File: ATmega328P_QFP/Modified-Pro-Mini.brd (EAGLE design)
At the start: 18.3 x 33.5 mm, 17 parts, among them Q1 8/16/20MHz, U1 ATMEGA328

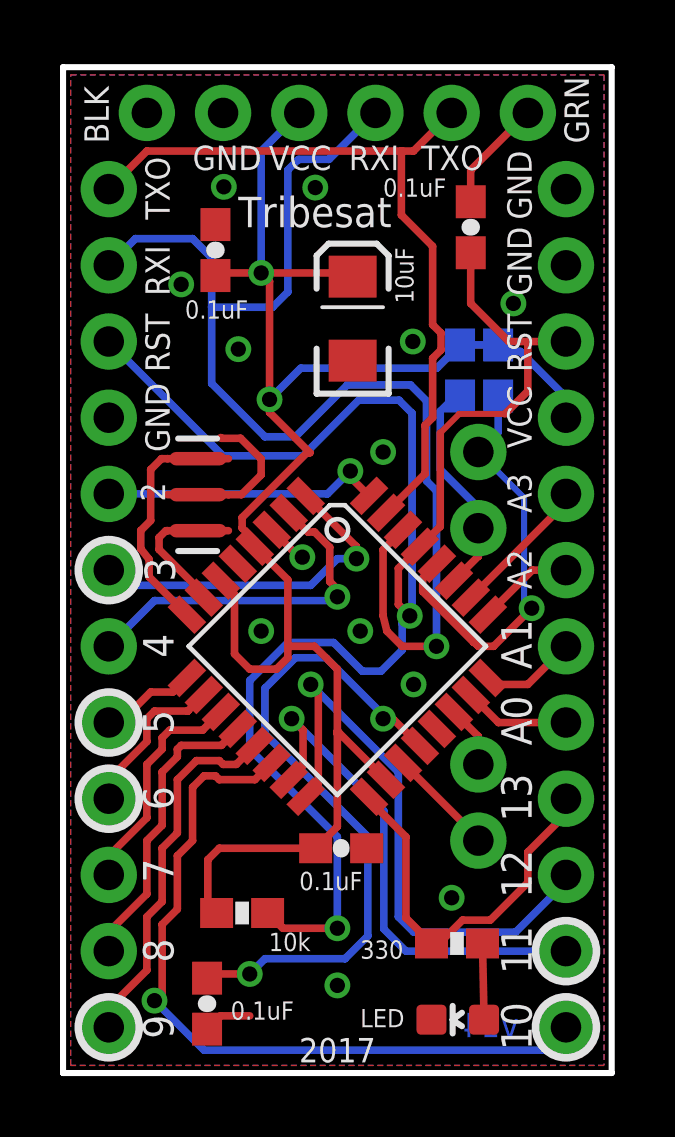
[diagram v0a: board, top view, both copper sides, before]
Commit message: Slight adjustments to prevent text from overlapping copper
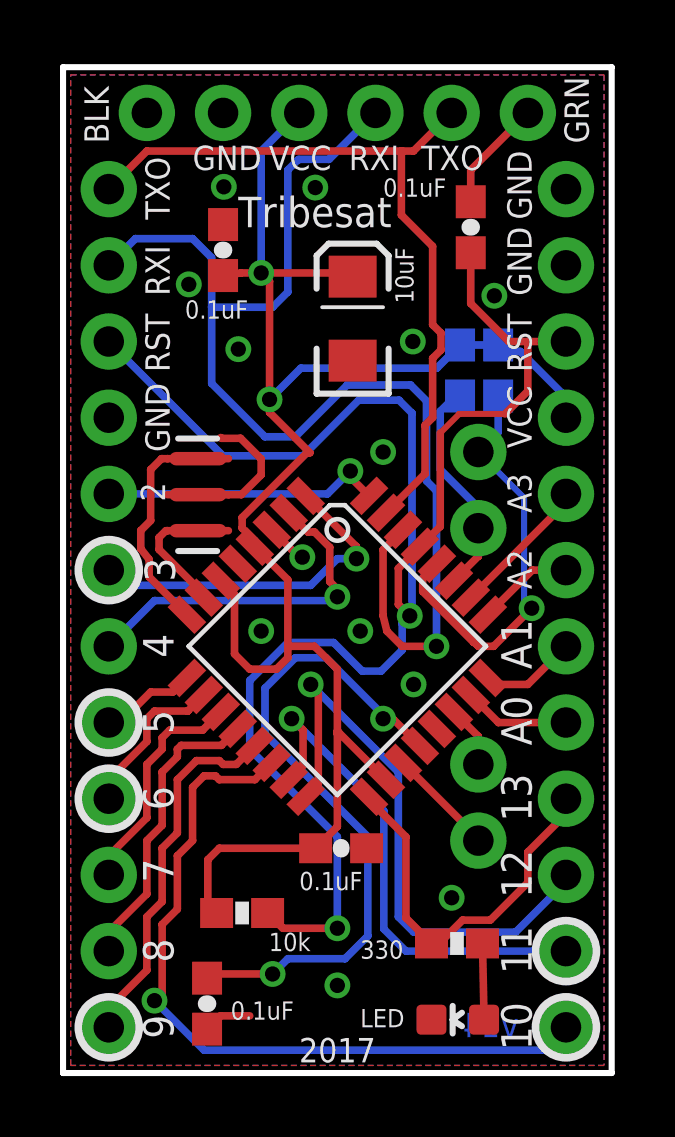
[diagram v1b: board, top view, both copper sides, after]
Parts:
- moved C4 0.25 mm to (5.08, 27.2)
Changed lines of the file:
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@@
 <text x="10.414" y="28.956" size="0.6096" layer="21" font="vector" ratio="13">0.1uF</text>
 <text x="5.334" y="28.702" size="1.016" layer="22" font="vector" ratio="16" rot="MR180">Tribesat</text>
-<text x="14.224" y="24.892" size="0.8128" layer="22" font="vector" ratio="16" rot="MR0">ATmega328P QFP</text>
 <text x="11.43" y="25.4" size="0.6096" layer="21" font="vector" ratio="13" rot="R90">10uF</text>
 <text x="3.81" y="24.892" size="0.6096" layer="21" font="vector" ratio="13">0.1uF</text>
-<text x="9.398" y="22.86" size="0.8128" layer="22" font="vector" ratio="17" rot="MR0" align="center">Test
+<text x="13.462" y="24.638" size="0.762" layer="22" font="vector" ratio="20" distance="10" rot="MR0">ATmega328P QFP</text>
+<text x="9.144" y="23.114" size="0.7366" layer="22" font="vector" ratio="20" distance="19" rot="MR0" align="center">Test
 Design
 V1.0</text>
@@
 <attribute name="VALUE" x="8.066" y="25.3" size="0.4064" layer="27" rot="R90"/>
 </element>
-<element name="C4" library="SparkFun" package="0603-CAP" value="0.1uF" x="4.826" y="27.178" smashed="yes" rot="R270">
-<attribute name="VALUE" x="3.683" y="28.194" size="0.4064" layer="27" font="vector" rot="R270"/>
+<element name="C4" library="SparkFun" package="0603-CAP" value="0.1uF" x="5.08" y="27.178" smashed="yes" rot="R270">
+<attribute name="VALUE" x="3.937" y="28.194" size="0.4064" layer="27" font="vector" rot="R270"/>
 </element>
 </elements>
@@
 <via x="10.414" y="20.447" extent="1-16" drill="0.508"/>
 <via x="6.35" y="14.478" extent="1-16" drill="0.508"/>
-<via x="14.7574" y="25.4" extent="1-16" drill="0.508"/>
+<via x="14.1224" y="25.654" extent="1-16" drill="0.508"/>
 <via x="7.7216" y="16.9418" extent="1-16" drill="0.508"/>
-<via x="3.683" y="26.035" extent="1-16" drill="0.508"/>
+<via x="3.937" y="26.035" extent="1-16" drill="0.508"/>
 <via x="11.4046" y="24.13" extent="1-16" drill="0.508"/>
 <polygon width="0.254" layer="1" isolate="0.3048">
@@
 <wire x1="10.414" y1="11.557" x2="10.7372" y2="11.557" width="0.254" layer="1"/>
 <via x="10.414" y="11.557" extent="1-16" drill="0.508"/>
-<wire x1="9.144" y1="3.556" x2="6.477" y2="3.556" width="0.254" layer="16"/>
-<wire x1="6.477" y1="3.556" x2="5.969" y2="3.048" width="0.254" layer="16"/>
-<via x="5.969" y="3.048" extent="1-16" drill="0.508"/>
-<wire x1="5.969" y1="3.048" x2="4.6872" y2="3.048" width="0.254" layer="1"/>
+<wire x1="9.144" y1="3.556" x2="7.239" y2="3.556" width="0.254" layer="16"/>
+<wire x1="7.239" y1="3.556" x2="6.731" y2="3.048" width="0.254" layer="16"/>
+<via x="6.731" y="3.048" extent="1-16" drill="0.508"/>
+<wire x1="6.731" y1="3.048" x2="4.6872" y2="3.048" width="0.254" layer="1"/>
 <wire x1="4.6872" y1="3.048" x2="4.5466" y2="2.9074" width="0.254" layer="1"/>
 <wire x1="11.64248125" y1="10.651828125" x2="10.737309375" y2="11.557" width="0.254" layer="1"/>
@@
 <contactref element="C13" pad="A"/>
 <contactref element="C4" pad="2"/>
-<wire x1="6.35" y1="26.416" x2="4.914" y2="26.416" width="0.254" layer="1"/>
-<wire x1="4.914" y1="26.416" x2="4.826" y2="26.328" width="0.254" layer="1"/>
+<wire x1="6.35" y1="26.416" x2="5.676" y2="26.416" width="0.254" layer="1"/>
+<wire x1="5.676" y1="26.416" x2="5.08" y2="26.328" width="0.254" layer="1"/>
 <wire x1="6.35" y1="26.416" x2="9.274" y2="26.416" width="0.254" layer="1"/>
 <wire x1="9.274" y1="26.416" x2="9.398" y2="26.292" width="0.254" layer="1"/>
